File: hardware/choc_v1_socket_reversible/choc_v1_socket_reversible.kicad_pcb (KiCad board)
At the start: 2 copper layers, 4.3 x 4.4 mm, 76 parts, among them J1 Conn_01x12_MountingPin, J2 Conn_01x12_MountingPin, SW00 SW_Push, SW01 SW_Push, SW02 SW_Push, SW03 SW_Push, SW04 SW_Push, SW05 SW_Push, SW10 SW_Push, SW11 SW_Push, SW12 SW_Push, SW13 SW_Push, SW14 SW_Push, SW15 SW_Push, SW20 SW_Push, SW21 SW_Push, SW22 SW_Push, SW23 SW_Push, SW24 SW_Push, SW25 SW_Push, SW30 SW_Push, SW31 SW_Push, SW32 SW_Push, SW33 SW_Push, SW34 SW_Push, SW35 SW_Push, SW36 SW_Push, SW37 SW_Push, U1 CH582, U2 74HC165, U4 74HC165

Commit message: Updated python script so it can be used as plugin; Updated connect_row()
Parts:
- turned LED01 to 0 degrees
- turned LED03 to 0 degrees
- turned LED05 to 0 degrees
- turned LED10 to 180 degrees
- turned LED12 to 180 degrees
- turned LED14 to 180 degrees
- turned LED21 to 0 degrees
- turned LED23 to 0 degrees
- turned LED25 to 0 degrees
- turned LED30 to 180 degrees
- turned LED32 to 180 degrees
- turned LED34 to 180 degrees
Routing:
- net Net-(LED20-DOUT): track 2.00 -> 20.2 mm
- net Net-(LED00-DOUT): track 2.00 -> 20.2 mm
- net COL0: track 77.8 -> 63.8 mm

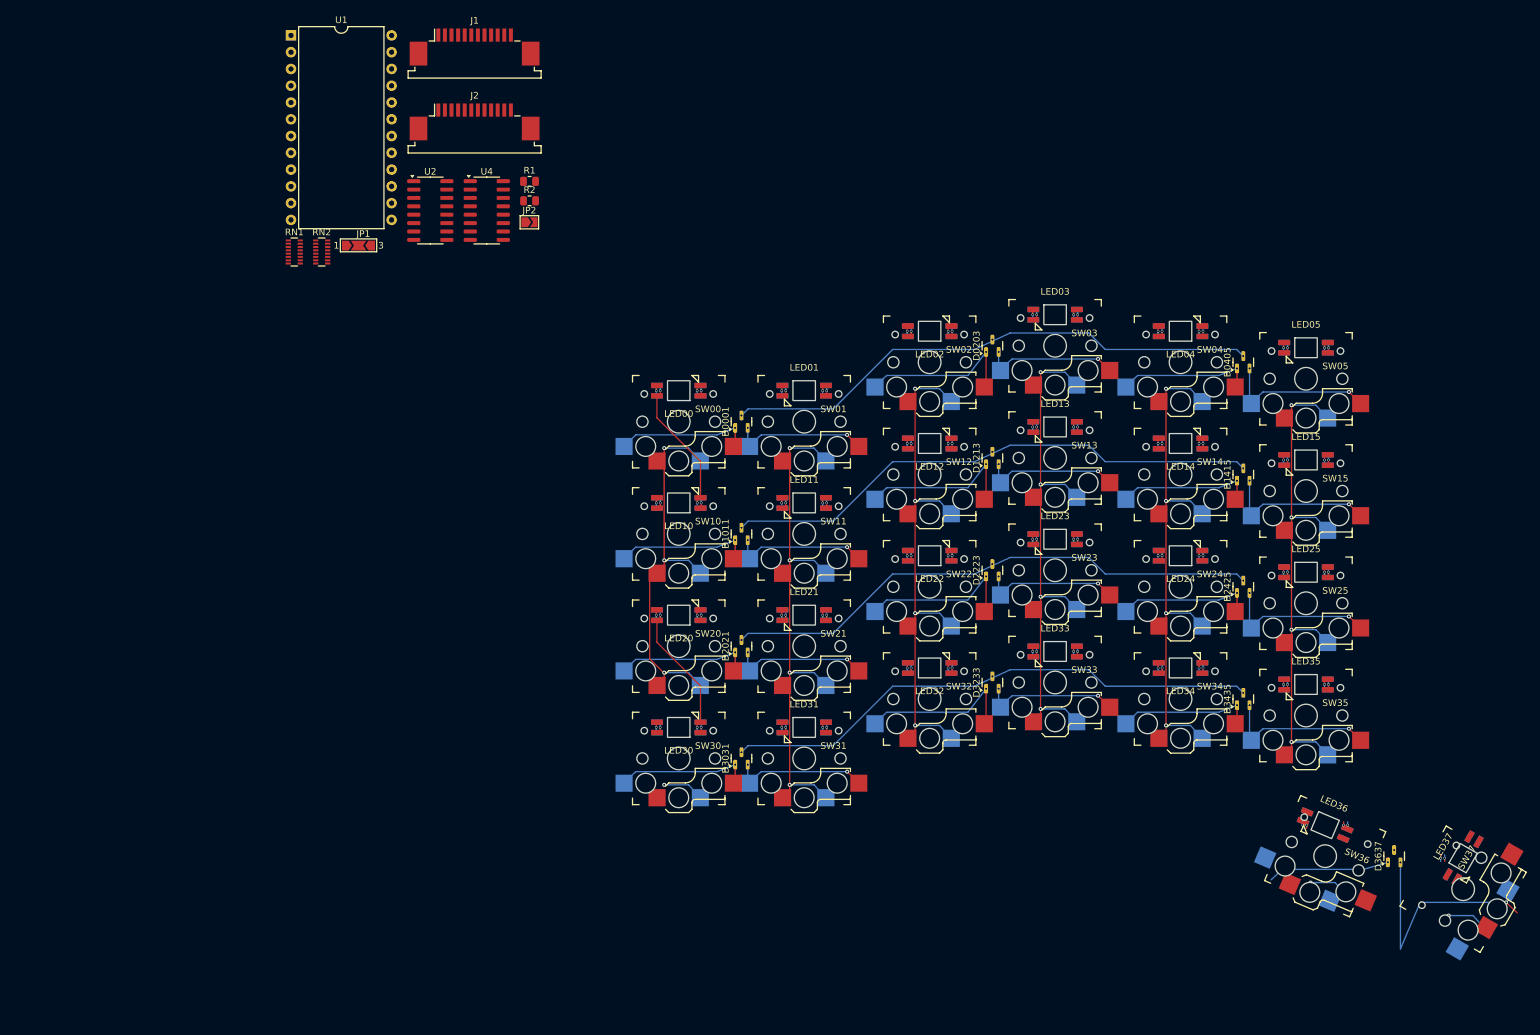
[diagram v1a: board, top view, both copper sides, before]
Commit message: Updated schematic and layout, todo: thumb cluster & MCU place and route
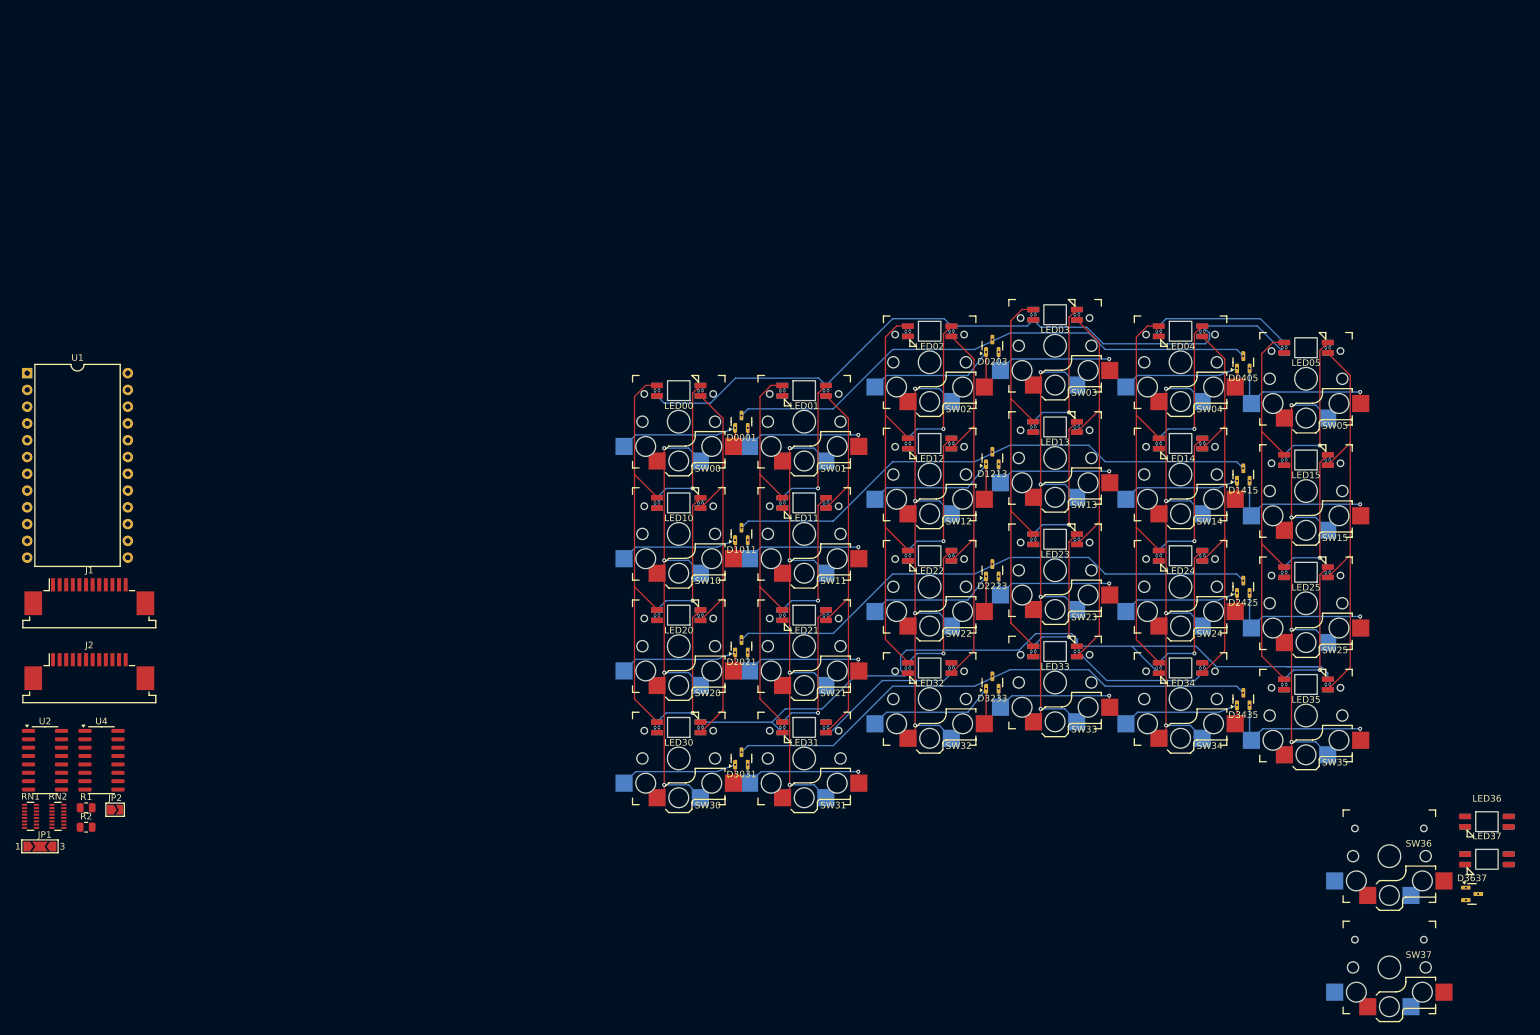
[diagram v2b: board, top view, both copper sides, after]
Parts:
- moved R1 116.2 mm to (-29.7, 118.5)
- moved R2 116.2 mm to (-29.7, 121.4)
- moved JP2 108.9 mm to (-25.4, 118.8)
- moved JP1 103.0 mm to (-36.7, 124.3)
- moved J1 101.7 mm to (-29.3, 86.5)
- moved J2 101.7 mm to (-29.3, 97.8)
- moved U2 101.7 mm to (-36.0, 111.3)
- moved U4 101.7 mm to (-27.4, 111.3)
- moved RN1 94.3 mm to (-38.2, 119.8)
- moved RN2 94.3 mm to (-34.0, 119.8)
- moved U1 64.9 mm to (-38.7, 52.6)
- moved LED36 24.5 mm to (182.4, 120.6), turned to 0 degrees
- moved SW37 16.3 mm to (167.6, 142.7), turned to 0 degrees
- moved D3637 13.1 mm to (180.1, 131.5), turned to 0 degrees
- moved SW36 9.72 mm to (167.6, 125.8), turned to 0 degrees
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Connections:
- LED01 pad 1: Net-(LED00-DIN) -> Net-(LED01-DOUT)
- LED01 pad 3: Net-(LED01-DIN) -> Net-(LED00-DOUT)
- LED02 pad 1: Net-(LED01-DIN) -> Net-(LED02-DOUT)
- LED04 pad 1: Net-(LED03-DIN) -> Net-(LED04-DOUT)
- LED10 pad 1: Net-(LED10-DOUT) -> Net-(LED00-DIN)
- LED10 pad 3: Net-(LED00-DOUT) -> Net-(LED10-DIN)
- LED11 pad 3: Net-(LED10-DOUT) -> Net-(LED01-DOUT)
- LED12 pad 3: Net-(LED11-DOUT) -> Net-(LED02-DOUT)
- LED13 pad 1: Net-(LED13-DOUT) -> Net-(LED03-DIN)
- LED13 pad 3: Net-(LED12-DOUT) -> Net-(LED13-DIN)
- LED14 pad 3: Net-(LED13-DOUT) -> Net-(LED04-DOUT)
- LED15 pad 1: Net-(LED15-DOUT) -> Net-(LED05-DIN)
- LED15 pad 3: Net-(LED14-DOUT) -> Net-(LED15-DIN)
- LED20 pad 1: Net-(LED20-DOUT) -> Net-(LED10-DIN)
- LED21 pad 1: Net-(LED20-DIN) -> Net-(LED21-DOUT)
- LED21 pad 3: Net-(LED21-DIN) -> Net-(LED11-DOUT)
- LED22 pad 1: Net-(LED21-DIN) -> Net-(LED22-DOUT)
- LED22 pad 3: Net-(LED22-DIN) -> Net-(LED12-DOUT)
- LED23 pad 1: Net-(LED22-DIN) -> Net-(LED13-DIN)
- LED24 pad 1: Net-(LED23-DIN) -> Net-(LED24-DOUT)
- LED24 pad 3: Net-(LED24-DIN) -> Net-(LED14-DOUT)
- LED25 pad 1: Net-(LED24-DIN) -> Net-(LED15-DIN)
- LED25 pad 3: Net-(LED15-DOUT) -> Net-(LED25-DIN)
- LED30 pad 1: Net-(LED30-DOUT) -> Net-(LED20-DIN)
- LED30 pad 3: Net-(LED20-DOUT) -> Net-(LED30-DIN)
- LED31 pad 3: Net-(LED30-DOUT) -> Net-(LED21-DOUT)
- LED32 pad 1: Net-(LED32-DOUT) -> Net-(LED31-DOUT)
- LED32 pad 3: Net-(LED31-DOUT) -> Net-(LED22-DOUT)
- LED33 pad 1: Net-(LED33-DOUT) -> Net-(LED23-DIN)
- LED33 pad 3: Net-(LED32-DOUT) -> Net-(LED33-DIN)
- LED34 pad 1: Net-(LED34-DOUT) -> Net-(LED33-DIN)
- LED34 pad 3: Net-(LED33-DOUT) -> Net-(LED24-DOUT)
- LED35 pad 1: Net-(LED35-DOUT) -> Net-(LED25-DIN)
- LED35 pad 3: Net-(LED34-DOUT) -> Net-(LED35-DIN)
- LED36 pad 3: Net-(LED35-DOUT) -> Net-(LED30-DIN)
- R2 pad 1: Net-(LED05-DIN) -> Net-(LED35-DIN)
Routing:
- net +5V: track 24.0 -> 530.3 mm
- net GND: track 24.0 -> 516.9 mm
- net Net-(D3637-A-Pad2): track 36.1 -> 0.00 mm, vias 1 -> 0
- net Net-(LED04-DOUT): track 0.00 -> 24.1 mm, vias 0 -> 3
- net Net-(LED25-DIN): track 0.00 -> 24.1 mm, vias 0 -> 3
- net Net-(LED24-DOUT): track 0.00 -> 24.1 mm, vias 0 -> 3
- net Net-(LED15-DIN): track 0.00 -> 24.1 mm, vias 0 -> 3
- net Net-(LED10-DIN): track 0.00 -> 24.1 mm, vias 0 -> 3
- net Net-(LED02-DOUT): track 0.00 -> 24.1 mm, vias 0 -> 3
- net Net-(LED22-DOUT): track 0.00 -> 24.1 mm, vias 0 -> 3
- net Net-(LED21-DOUT): track 0.00 -> 24.1 mm, vias 0 -> 3
- net Net-(LED13-DIN): track 0.00 -> 24.1 mm, vias 0 -> 3
- net Net-(LED01-DOUT): track 0.00 -> 24.1 mm, vias 0 -> 3
- net Net-(LED05-DIN): track 1.00 -> 24.1 mm, vias 1 -> 3
- net Net-(LED33-DIN): track 0.00 -> 23.0 mm, vias 0 -> 2
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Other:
- board size 4.3 x 4.4 mm -> 3.4 x 3 mm

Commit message: Updated reference
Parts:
- removed RN1, RN2: R_Pack08, Resistor_SMD:R_Array_Convex_8x0602
- removed U2, U4: 74HC165, Package_SO:SOP-16_3.9x9.9mm_P1.27mm
- added RN_LEFT1: R_Pack08, Resistor_SMD:R_Array_Convex_8x0602, F.Cu at (175.3, 110.7)
- added RN_RIGHT1: R_Pack08, Resistor_SMD:R_Array_Convex_8x0602, F.Cu at (179.5, 110.7)
- added SR_LEFT1: 74HC165, Package_SO:SOP-16_3.9x9.9mm_P1.27mm, F.Cu at (177.5, 102.2)
- added SR_RIGHT1: 74HC165, Package_SO:SOP-16_3.9x9.9mm_P1.27mm, F.Cu at (186.1, 102.2)
- moved J1 213.7 mm to (184.2, 77.5)
- moved J2 213.7 mm to (184.2, 88.8)
- moved JP1 213.7 mm to (176.8, 115.3)
- moved JP2 213.7 mm to (188.1, 109.7)
- moved R1 213.7 mm to (183.8, 109.4)
- moved R2 213.7 mm to (183.8, 112.4)
- moved U1 213.7 mm to (174.8, 43.6)
- moved D3637 8.34 mm to (172.7, 135.3)
- moved LED36 8.34 mm to (174.9, 124.3)
- moved LED37 8.34 mm to (174.9, 130.0)
- moved SW36 8.34 mm to (160.2, 129.6)
- moved SW37 8.34 mm to (160.2, 146.4)
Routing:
- net +5V: track 530.3 -> 407.3 mm
- net GND: track 516.9 -> 407.3 mm
- net Net-(LED31-DOUT): track 24.7 -> 2.00 mm
- net Net-(LED33-DIN): track 23.0 -> 2.00 mm
- net Net-(LED04-DIN): track 23.0 -> 2.00 mm

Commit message: Clean up
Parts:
- J1, JP1, R1, R2, RN_LEFT1, SR_LEFT1: moved to B.Cu
- moved R1 62.2 mm to (165.0, 50.1)
- moved JP1 61.0 mm to (176.3, 54.2)
- moved R2 55.1 mm to (176.4, 57.8)
- moved LED36 25.5 mm to (149.9, 119.2)
- moved SW37 20.2 mm to (167.3, 127.5)
- moved D3637 19.9 mm to (159.6, 120.2), turned to 90 degrees
- moved JP2 16.5 mm to (175.6, 120.5), turned to 90 degrees
- moved RN_LEFT1 12.5 mm to (186.3, 104.7), turned to -90 degrees
- moved SR_RIGHT1 12.5 mm to (174.6, 107.2), turned to 90 degrees
- moved SW36 11.6 mm to (150.0, 123.9)
- moved RN_RIGHT1 10.4 mm to (186.3, 102.8), turned to 90 degrees
- moved LED37 10.3 mm to (167.6, 122.8)
- moved J1 7.56 mm to (183.9, 85.0), turned to 135 degrees
- moved U1 6.50 mm to (168.4, 44.3)
- moved J2 3.83 mm to (183.9, 85.0), turned to -45 degrees
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
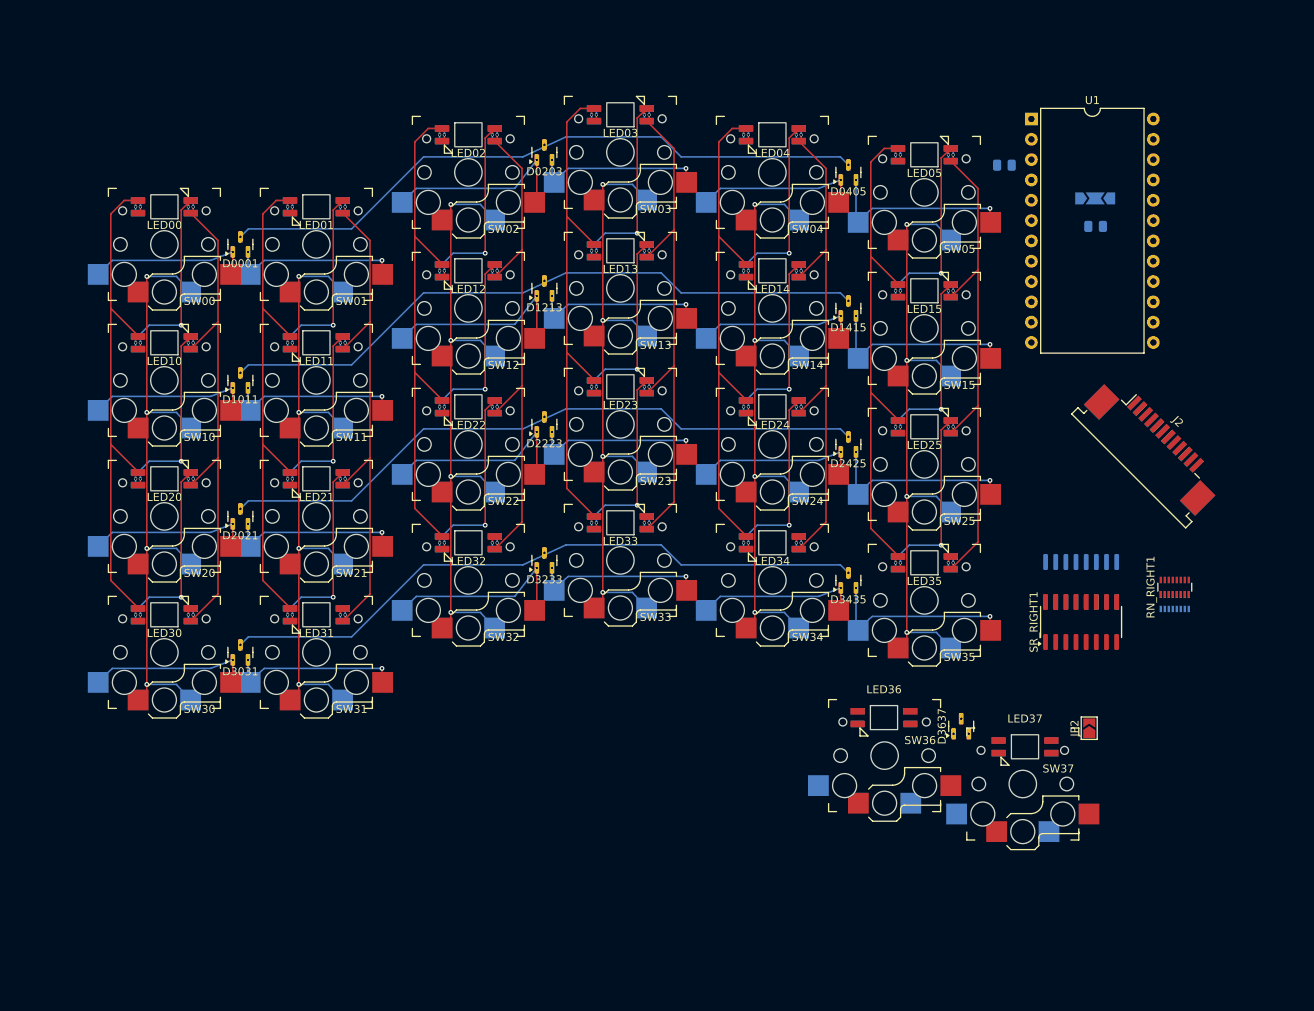
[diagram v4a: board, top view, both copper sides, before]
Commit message: Connected everything and added copper pour
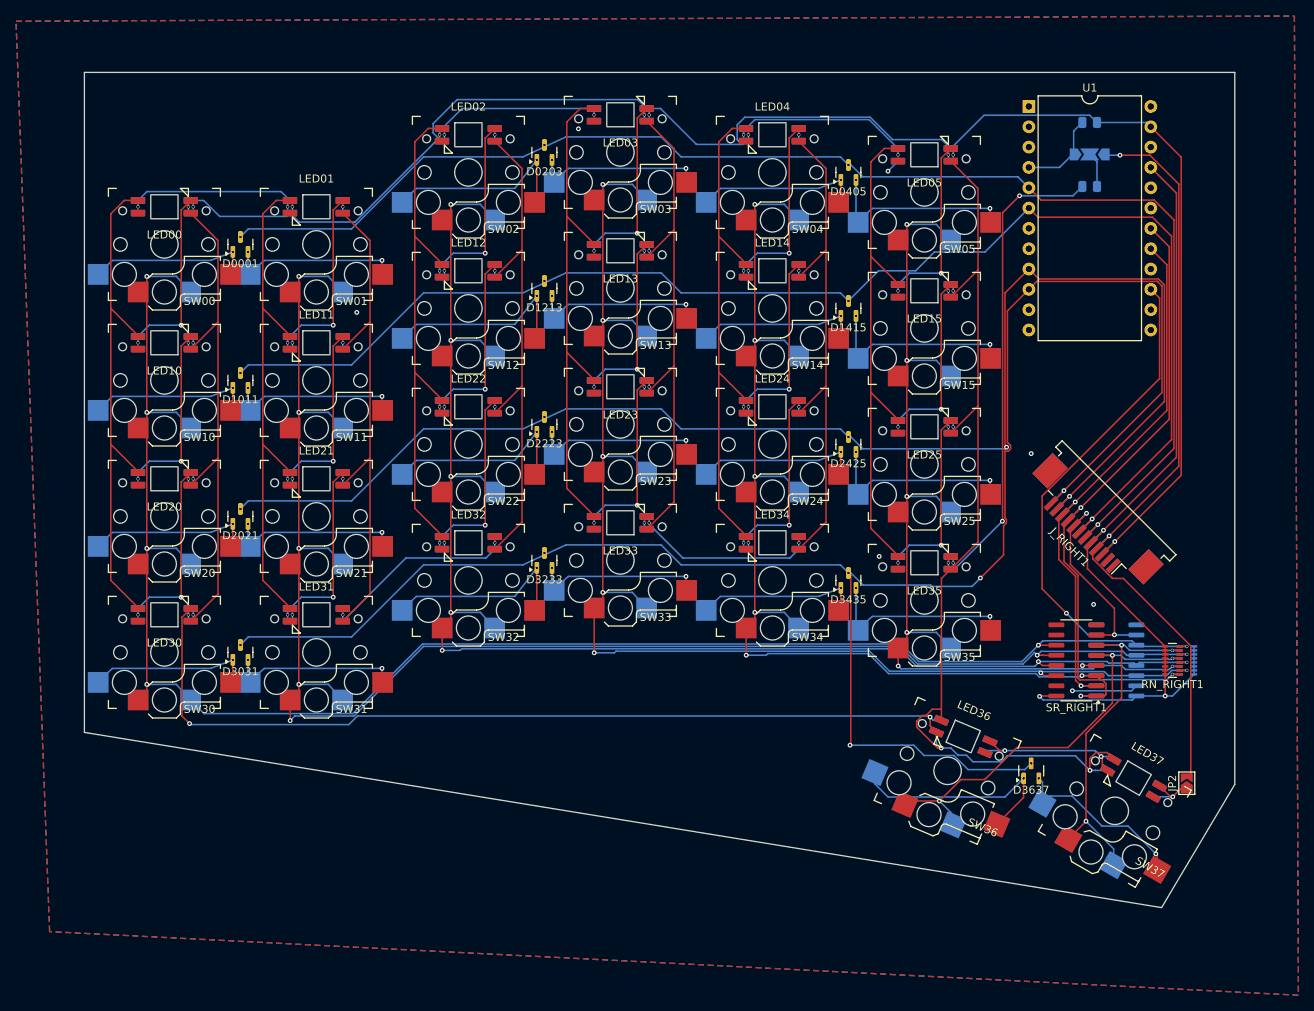
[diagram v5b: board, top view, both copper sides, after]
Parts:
- removed J1, J2: Conn_01x12_MountingPin, Connector_FFC-FPC:TE_1-84952-2_1x12-1MP_P1.0mm_Horizontal
- added J_LEFT1: Conn_01x12_MountingPin, Connector_FFC-FPC:TE_1-84952-2_1x12-1MP_P1.0mm_Horizontal, B.Cu at (176.0, 95.0)
- added J_RIGHT1: Conn_01x12_MountingPin, Connector_FFC-FPC:TE_1-84952-2_1x12-1MP_P1.0mm_Horizontal, F.Cu at (176.0, 95.0)
- moved LED37 14.1 mm to (181.2, 126.7), turned to -30 degrees
- moved JP2 14.0 mm to (187.8, 127.3)
- moved SW37 12.0 mm to (178.8, 130.8), turned to -30 degrees
- moved R1 11.9 mm to (175.7, 44.8), turned to 180 degrees
- moved SR_LEFT1 10.7 mm to (179.0, 112.0), turned to 0 degrees
- moved D3637 10.4 mm to (168.3, 125.8)
- moved LED36 10.2 mm to (159.8, 121.5), turned to -23 degrees
- moved RN_RIGHT1 9.15 mm to (186.0, 112.0), turned to 180 degrees
- moved SW36 8.10 mm to (157.9, 125.8), turned to -23 degrees
- moved RN_LEFT1 7.48 mm to (187.8, 112.0), turned to 0 degrees
- moved JP1 5.53 mm to (175.7, 48.8)
- moved R2 5.04 mm to (175.7, 52.8)
- moved SR_RIGHT1 4.84 mm to (174.0, 112.0), turned to 180 degrees
- moved U1 1.60 mm to (168.1, 42.8)
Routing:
- net +5V: track 407.3 -> 682.1 mm, vias 24 -> 27
- net ROW3: track 82.1 -> 237.5 mm, vias 0 -> 3
- net COL0: track 77.8 -> 211.8 mm, vias 4 -> 6
- net COL1: track 77.8 -> 201.5 mm, vias 4 -> 7
- net Net-(LED30-DIN): track 1.00 -> 113.7 mm, vias 1 -> 3
- net +3V3: track 0.00 -> 104.1 mm, vias 0 -> 3
- net COL2: track 77.8 -> 178.7 mm, vias 4 -> 7
- net ROW2: track 82.1 -> 179.8 mm, vias 0 -> 2
- net LED_R: track 0.00 -> 96.9 mm, vias 0 -> 2
- net ROW1: track 82.1 -> 172.8 mm, vias 0 -> 1
- net ROW0: track 82.1 -> 172.2 mm, vias 0 -> 1
- net COL3: track 77.8 -> 162.2 mm, vias 4 -> 7
- net SCS: track 0.00 -> 76.0 mm, vias 0 -> 2
- net SCK0: track 0.00 -> 67.7 mm, vias 0 -> 2
- net COL4: track 77.8 -> 139.9 mm, vias 4 -> 7
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- added copper zone on B.Cu, net GND
- added copper zone on F.Cu, net GND
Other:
- board size 3.4 x 3 mm -> 143.8 x 104.4 mm
